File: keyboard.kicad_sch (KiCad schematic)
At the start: 5 parts, among them U1 Teensy4.1, U101 CAT24C256

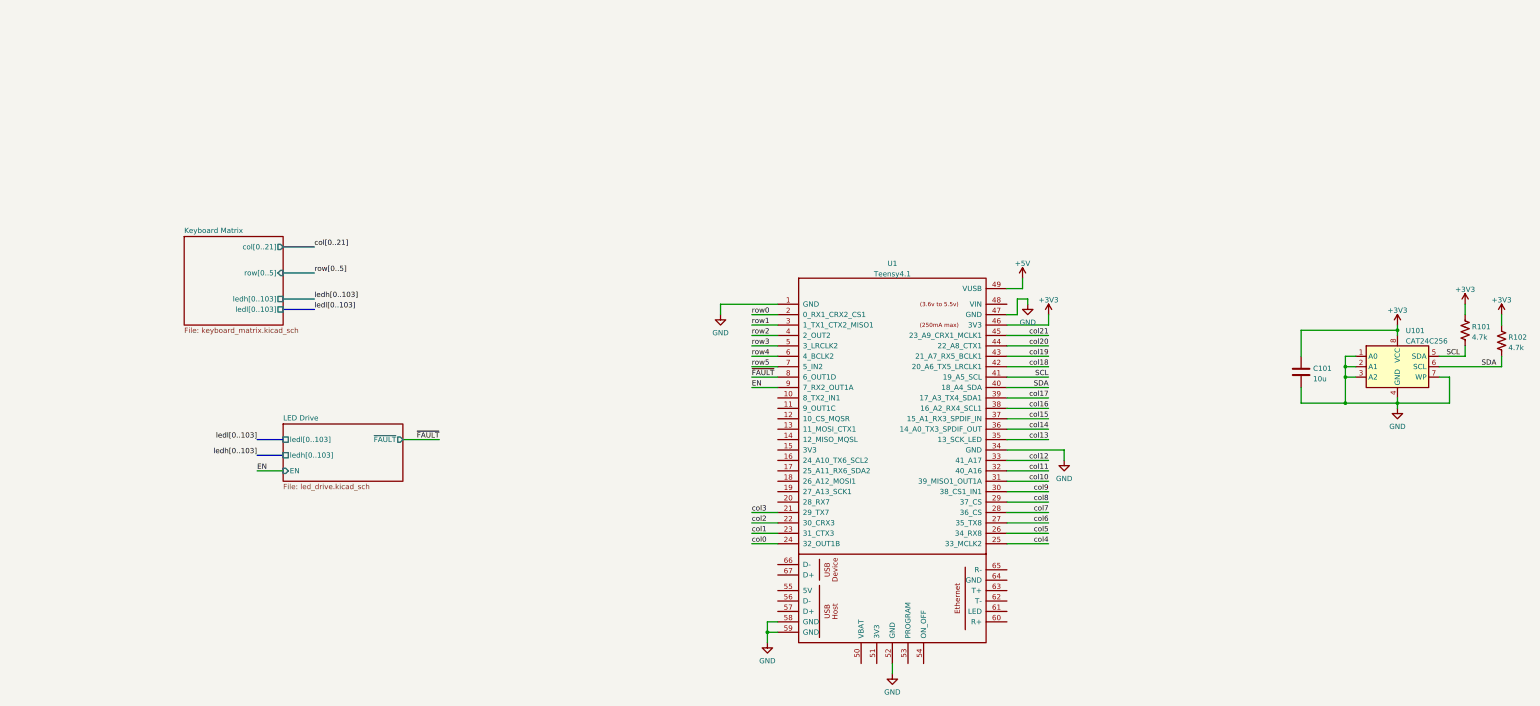
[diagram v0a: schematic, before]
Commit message: Move load switch to main sheet
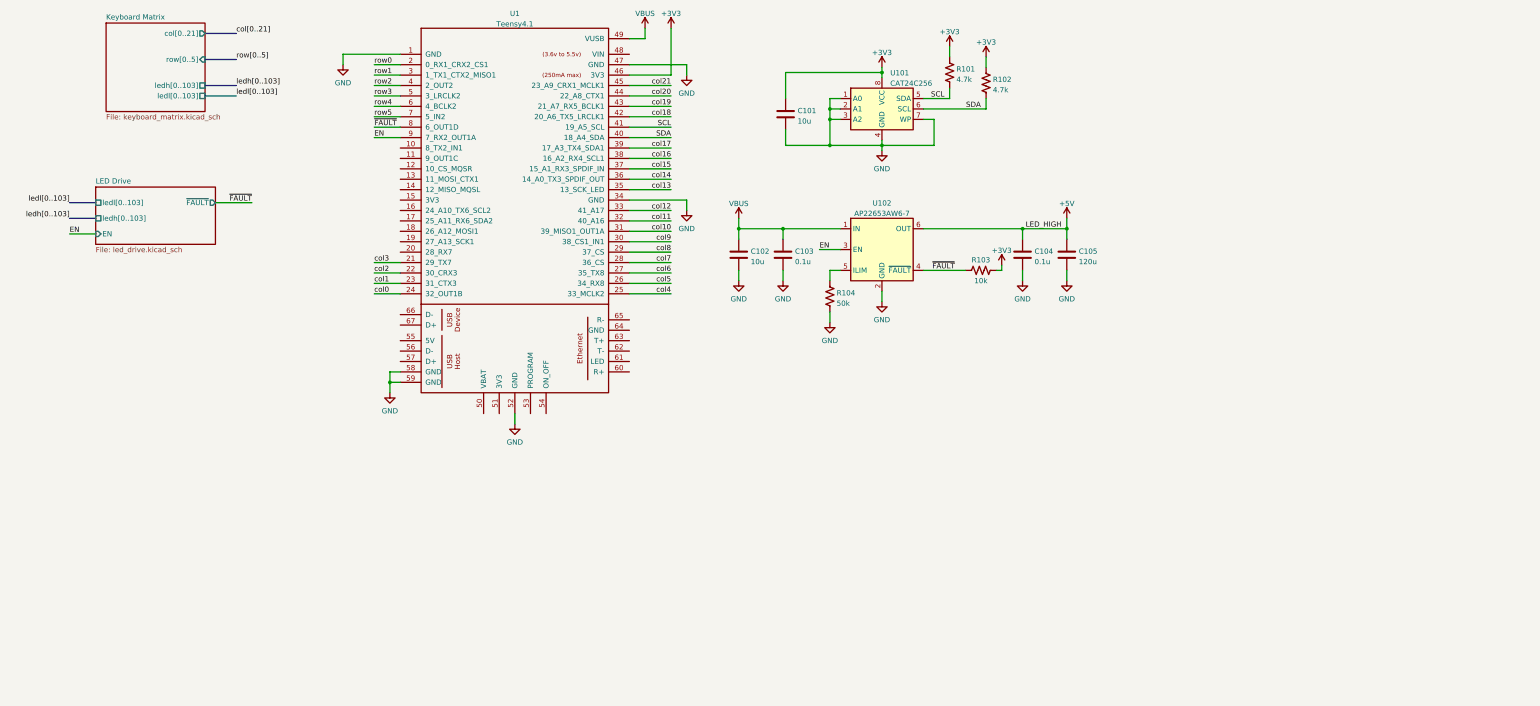
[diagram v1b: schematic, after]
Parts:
- added C102: 10u, Capacitor_SMD:C_0603_1608Metric, symbol Device:C
- added C103, C104: 0.1u, Capacitor_SMD:C_0603_1608Metric, symbol Device:C
- added C105: 120u, Capacitor_SMD:C_0603_1608Metric, symbol Device:C
- added R103: 10k, Resistor_SMD:R_0603_1608Metric, symbol Device:R_US
- added R104: 50k, Resistor_SMD:R_0603_1608Metric, symbol Device:R_US
- added U102: AP22653AW6-7, Package_TO_SOT_SMD:SOT-23-6_Handsoldering, symbol Keyboard:AP22653AW6-7
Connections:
- net +3V3: now also R103.1
- net +5V: now also C104.1, C105.1, U102.6 (OUT); no longer U1.49 (VUSB)
- net EN: now also U102.3 (EN)
- net GND: now also C102.2, C103.2, C104.2, C105.2, R104.2, U102.2 (GND)
- net ~{FAULT}: now also R103.2, U102.4 (~{FAULT})
- new net: R104.1, U102.5 (ILIM)
- new net VBUS: C102.1, C103.1, U1.49 (VUSB), U102.1 (IN)
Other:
- moved on the sheet: C101, R101, R102, U1, U101

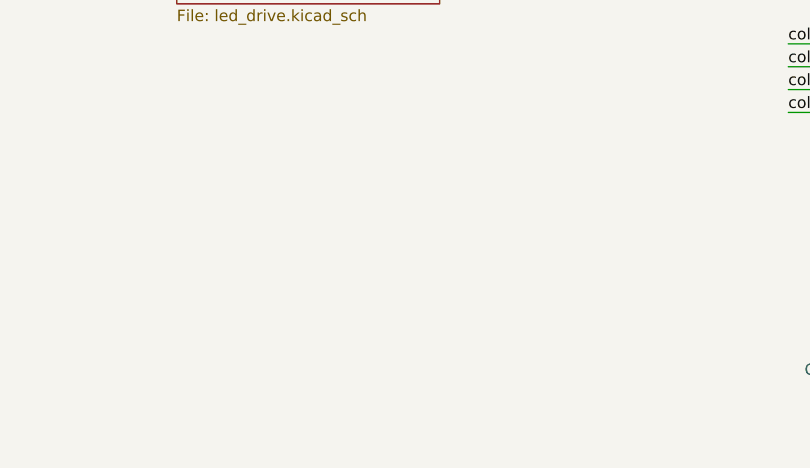
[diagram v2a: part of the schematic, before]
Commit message: Clean up board and add mounting holes
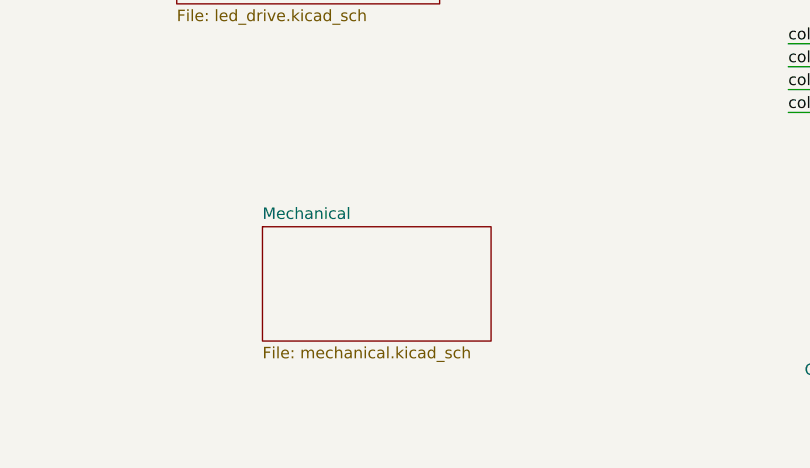
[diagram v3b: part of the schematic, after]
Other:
- added sheet Mechanical (mechanical.kicad_sch)
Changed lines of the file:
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@@
+    )
+  )
+  (sheet (at 45.085 121.92) (size 25.4 12.7) (fields_autoplaced)
+    (stroke (width 0.1524) (type solid) (color 0 0 0 0))
+    (fill (color 0 0 0 0.0000))
+    (property "Sheet name" "Mechanical" (id 0) (at 45.085 121.2084 0)
+      (effects (font (size 1.27 1.27)) (justify left bottom))
+    )
+    (property "Sheet file" "mechanical.kicad_sch" (id 1) (at 45.085 135.2046 0)
+      (effects (font (size 1.27 1.27)) (justify left top))
     )
   )
@@
     (path "/31bb8932-832f-42ce-a5dc-7daa763a98f8" (page "2"))
     (path "/b34db869-75de-41e1-87eb-fcf4a8830e98" (page "3"))
+    (path "/41caac07-142d-465b-b097-17388d01d1f7" (page "4"))
   )
   (symbol_instances
@@
       (reference "#PWR0120") (unit 1) (value "GND") (footprint "")
     )
+    (path "/41caac07-142d-465b-b097-17388d01d1f7/6ebac1cf-3474-4aff-9c58-529351e355a4"
+      (reference "#PWR0401") (unit 1) (value "GND") (footprint "")
+    )
+    (path "/41caac07-142d-465b-b097-17388d01d1f7/e8645cd3-b3df-4151-9c98-71b24adb97b9"
+      (reference "#PWR0402") (unit 1) (value "GND") (footprint "")
+    )
+    (path "/41caac07-142d-465b-b097-17388d01d1f7/77c97090-27b5-41a9-844f-1e83f544d1a3"
+      (reference "#PWR0403") (unit 1) (value "GND") (footprint "")
+    )
+    (path "/41caac07-142d-465b-b097-17388d01d1f7/aa8f0210-0e5c-4a4c-8c7e-2b17249bc063"
+      (reference "#PWR0404") (unit 1) (value "GND") (footprint "")
+    )
+    (path "/41caac07-142d-465b-b097-17388d01d1f7/ec19980a-8f14-4fa7-ac1f-ff80ef914a8d"
+      (reference "#PWR0405") (unit 1) (value "GND") (footprint "")
+    )
+    (path "/41caac07-142d-465b-b097-17388d01d1f7/ad923fee-8552-46df-9814-1f027e7fbf82"
+      (reference "#PWR0406") (unit 1) (value "GND") (footprint "")
+    )
+    (path "/41caac07-142d-465b-b097-17388d01d1f7/c443691d-64d4-4701-9087-37f6d1c5a3b6"
+      (reference "#PWR0407") (unit 1) (value "GND") (footprint "")
+    )
     (path "/b34db869-75de-41e1-87eb-fcf4a8830e98/7615f6fc-1913-4b11-a1af-f0d0bfa56aaa"
       (reference "#PWR03000") (unit 1) (value "GND") (footprint "")
@@
       (reference "D_103") (unit 1) (value "D") (footprint "Diode_SMD:D_SOD-123")
     )
+    (path "/41caac07-142d-465b-b097-17388d01d1f7/7b391dc8-24de-4f28-a444-145cb93e97e3"
+      (reference "H401") (unit 1) (value "MountingHole_Pad") (footprint "MountingHole:MountingHole_3.2mm_M3_Pad_Via")
+    )
+    (path "/41caac07-142d-465b-b097-17388d01d1f7/38cdd67c-5f04-4257-9905-c9ce088d900a"
+      (reference "H402") (unit 1) (value "MountingHole_Pad") (footprint "MountingHole:MountingHole_3.2mm_M3_Pad_Via")
+    )
+    (path "/41caac07-142d-465b-b097-17388d01d1f7/acfce364-9761-4a18-bda3-8e8bcec07037"
+      (reference "H403") (unit 1) (value "MountingHole_Pad") (footprint "MountingHole:MountingHole_3.2mm_M3_Pad_Via")
+    )
+    (path "/41caac07-142d-465b-b097-17388d01d1f7/4d44bbad-d20e-44c7-9490-8e466acf1a10"
+      (reference "H404") (unit 1) (value "MountingHole_Pad") (footprint "MountingHole:MountingHole_3.2mm_M3_Pad_Via")
+    )
+    (path "/41caac07-142d-465b-b097-17388d01d1f7/c07362b6-fc8f-47dd-a2f9-e92d5662744d"
+      (reference "H405") (unit 1) (value "MountingHole_Pad") (footprint "MountingHole:MountingHole_3.2mm_M3_Pad_Via")
+    )
+    (path "/41caac07-142d-465b-b097-17388d01d1f7/d21acf90-816d-4b7d-93a7-f396e34c4035"
+      (reference "H406") (unit 1) (value "MountingHole_Pad") (footprint "MountingHole:MountingHole_3.2mm_M3_Pad_Via")
+    )
+    (path "/41caac07-142d-465b-b097-17388d01d1f7/b8af778d-eb2a-4ad2-b5d8-b86fc173018f"
+      (reference "H407") (unit 1) (value "MountingHole_Pad") (footprint "MountingHole:MountingHole_3.2mm_M3_Pad_Via")
+    )
+    (path "/41caac07-142d-465b-b097-17388d01d1f7/034073a4-6f29-4b73-9814-952efa8271b2"
+      (reference "JP401") (unit 1) (value "SolderJumper_2_Open") (footprint "Jumper:SolderJumper-2_P1.3mm_Open_Pad1.0x1.5mm")
+    )
+    (path "/41caac07-142d-465b-b097-17388d01d1f7/d0d1b91a-cbd7-400b-9623-d9b1deeb05c7"
+      (reference "JP402") (unit 1) (value "SolderJumper_2_Open") (footprint "Jumper:SolderJumper-2_P1.3mm_Open_Pad1.0x1.5mm")
+    )
+    (path "/41caac07-142d-465b-b097-17388d01d1f7/98992259-93ca-4ab1-bfff-27184869d868"
+      (reference "JP403") (unit 1) (value "SolderJumper_2_Open") (footprint "Jumper:SolderJumper-2_P1.3mm_Open_Pad1.0x1.5mm")
+    )
+    (path "/41caac07-142d-465b-b097-17388d01d1f7/e4347102-09af-4e0d-a5c9-3dfa5db01bb4"
+      (reference "JP404") (unit 1) (value "SolderJumper_2_Open") (footprint "Jumper:SolderJumper-2_P1.3mm_Open_Pad1.0x1.5mm")
+    )
+    (path "/41caac07-142d-465b-b097-17388d01d1f7/40fd58e7-8364-4368-8f65-b49f2f07ab3f"
+      (reference "JP405") (unit 1) (value "SolderJumper_2_Open") (footprint "Jumper:SolderJumper-2_P1.3mm_Open_Pad1.0x1.5mm")
+    )
+    (path "/41caac07-142d-465b-b097-17388d01d1f7/8b4fe6fb-4738-4836-a839-00a05c2d9c93"
+      (reference "JP406") (unit 1) (value "SolderJumper_2_Open") (footprint "Jumper:SolderJumper-2_P1.3mm_Open_Pad1.0x1.5mm")
+    )
+    (path "/41caac07-142d-465b-b097-17388d01d1f7/18b9bb38-a0a8-4c47-8090-635ff77467c0"
+      (reference "JP407") (unit 1) (value "SolderJumper_2_Open") (footprint "Jumper:SolderJumper-2_P1.3mm_Open_Pad1.0x1.5mm")
+    )
     (path "/31bb8932-832f-42ce-a5dc-7daa763a98f8/a622e1d1-d9cf-4694-8dd4-655c72988216"
